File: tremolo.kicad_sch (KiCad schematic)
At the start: 29 parts, among them J1 Jack-DC, J4 Conn_01x01_Female, J5 Conn_01x01_Female, Q1 MMBT3904, SW1 SW_Push, SW2 SW_DIP_x02, U1 TAPLFO3, U2 L78L05_SOT89, U3 VTL5C, U4 TL072

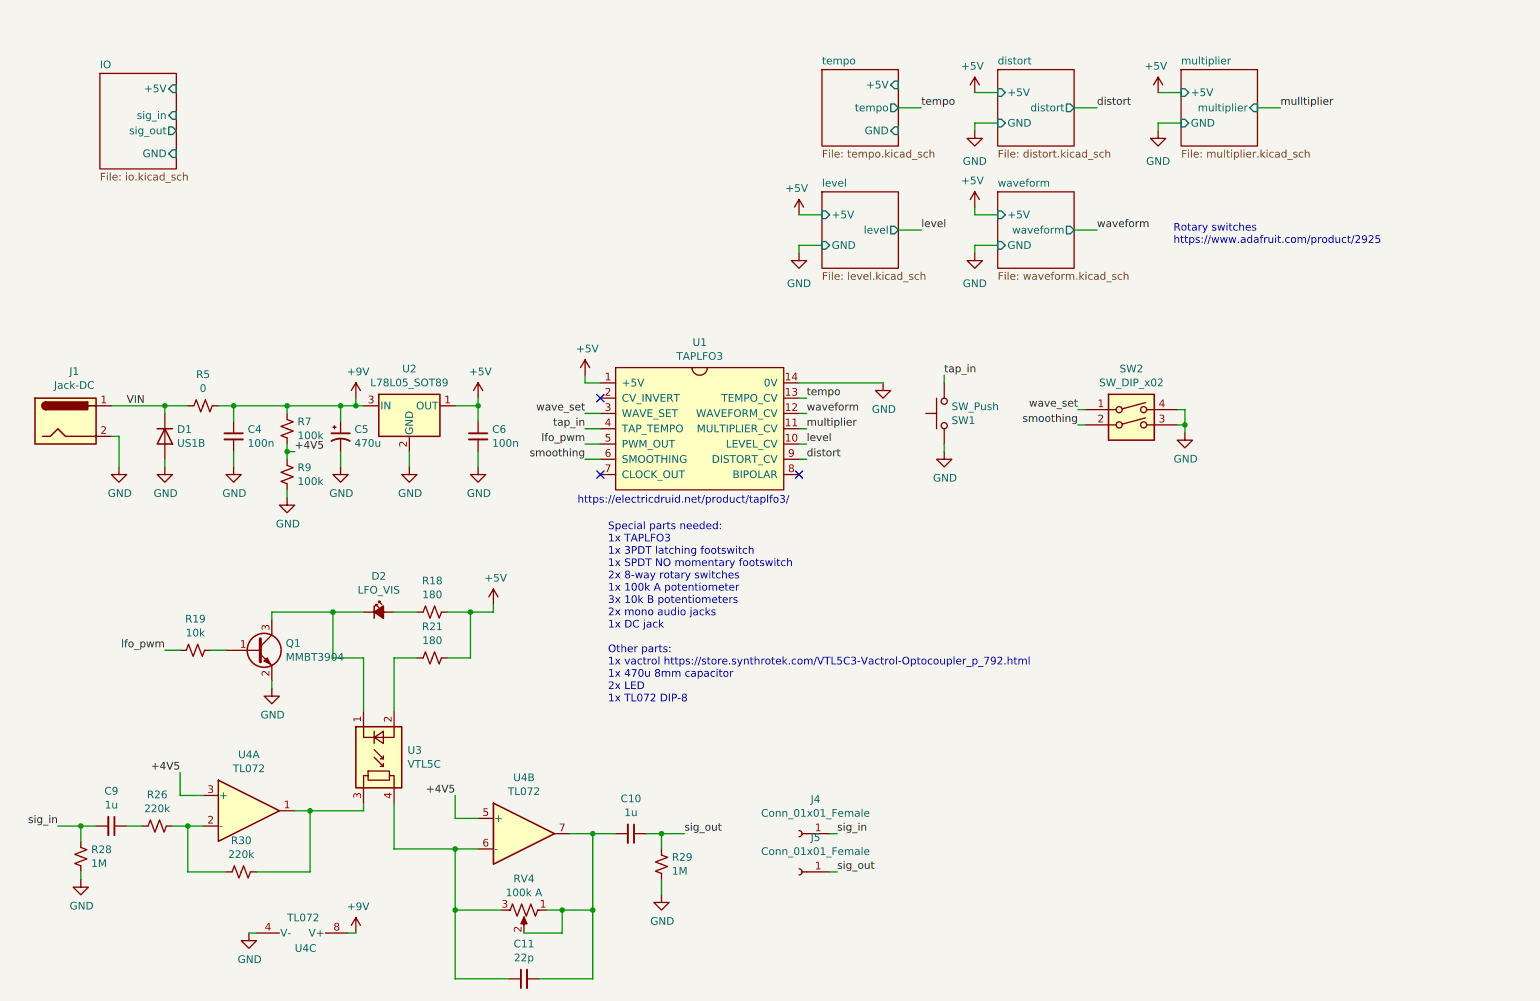
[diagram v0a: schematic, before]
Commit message: Separate IO from main board
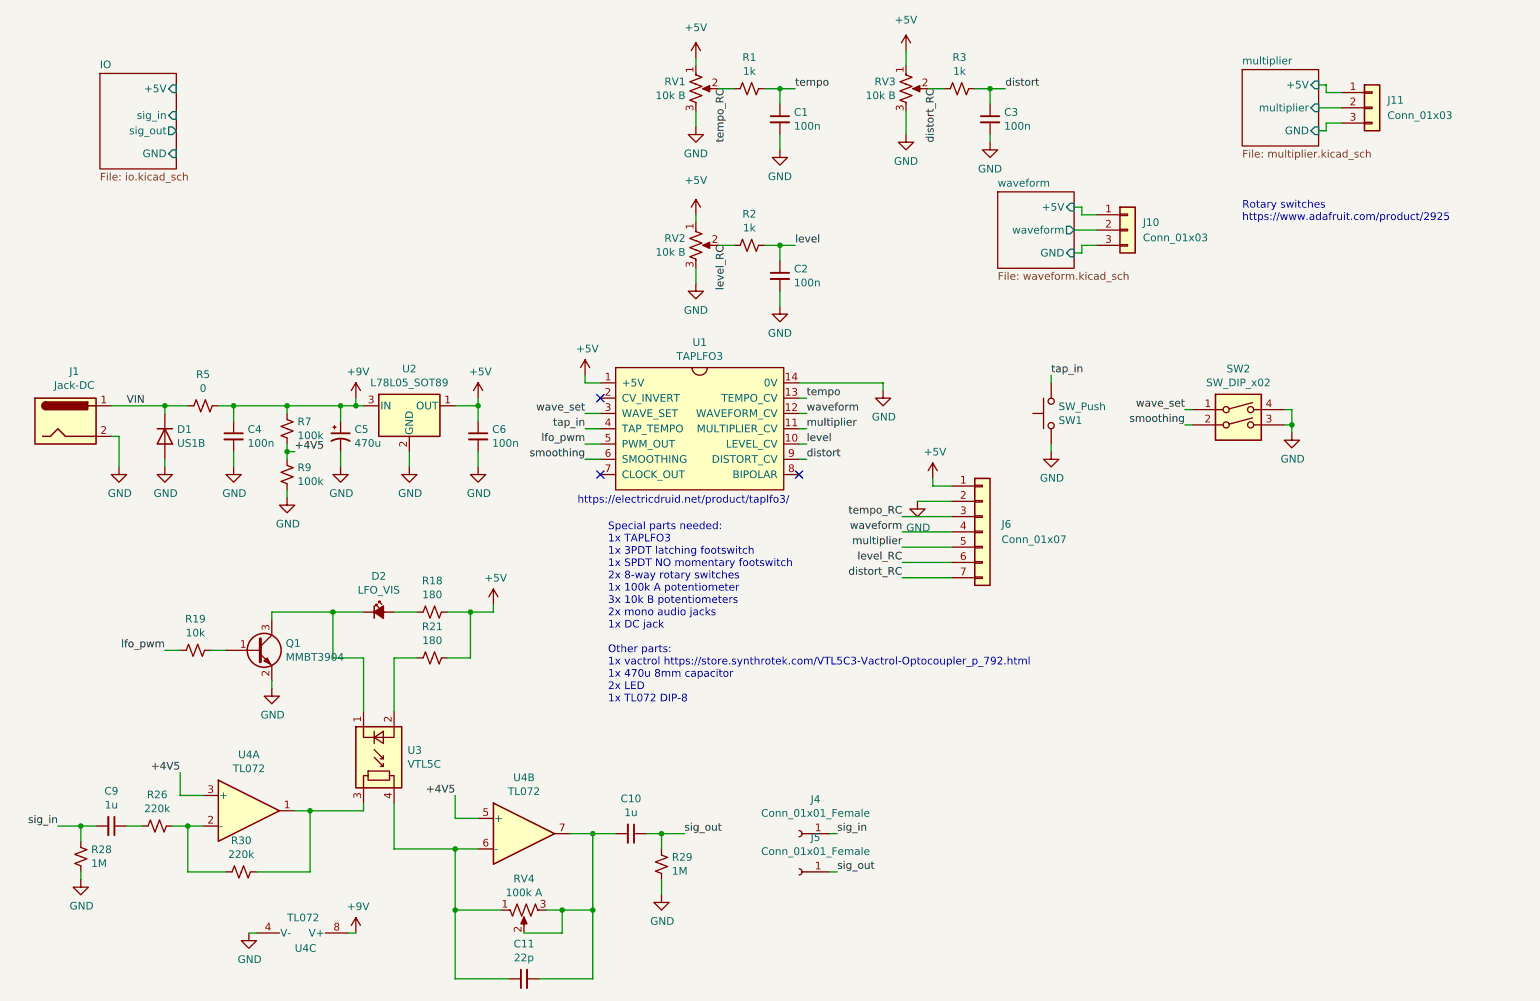
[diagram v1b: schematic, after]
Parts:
- added C1, C2, C3: 100n, Capacitor_SMD:C_0805_2012Metric, symbol Device:C_Small
- added J10, J11: Conn_01x03, Connector_PinHeader_2.54mm:PinHeader_1x03_P2.54mm_Vertical, symbol Connector_Generic:Conn_01x03
- added J6: Conn_01x07, Connector_PinHeader_2.54mm:PinHeader_1x07_P2.54mm_Vertical, symbol Connector_Generic:Conn_01x07
- added R1, R2, R3: 1k, Resistor_SMD:R_0805_2012Metric, symbol Device:R_Small_US
- added RV1, RV2, RV3: 10k B, Potentiometer_THT:Potentiometer_Alps_RK09L_Single_Vertical, symbol Device:R_Potentiometer_US
- RV4: footprint Potentiometer_THT:Potentiometer_Alps_RK09L_Single_Vertical -> Connector_PinHeader_2.54mm:PinHeader_1x02_P2.54mm_Vertical
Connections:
- net +5V: now also J6.1 (Pin_1), RV1.1, RV2.1, RV3.1
- net GND: now also C1.2, C2.2, C3.2, J6.2 (Pin_2), RV1.3, RV2.3, RV3.3
- net distort: now also C3.1, R3.2
- net level: now also C2.1, R2.2
- net multiplier: now also J6.5 (Pin_5)
- net tempo: now also C1.1, R1.2
- net waveform: now also J6.4 (Pin_4)
- net at C11.1, U3.4, U4.6 (-): now also RV4.1; no longer RV4.3
- net at C10.2, C11.2, RV4.2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: now also RV4.3; no longer RV4.1
- new net distort_RC: J6.7 (Pin_7), R3.1, RV3.2
- new net level_RC: J6.6 (Pin_6), R2.1, RV2.2
- new net multiplier/+5V: J11.1 (Pin_1)
- new net multiplier/GND: J11.3 (Pin_3)
- new net multiplier/multiplier: J11.2 (Pin_2)
- new net tempo_RC: J6.3 (Pin_3), R1.1, RV1.2
- new net waveform/+5V: J10.1 (Pin_1)
- new net waveform/GND: J10.3 (Pin_3)
- new net waveform/waveform: J10.2 (Pin_2)
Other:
- removed sheet distort
- removed sheet level
- removed sheet tempo
- moved on the sheet: RV4, SW1, SW2

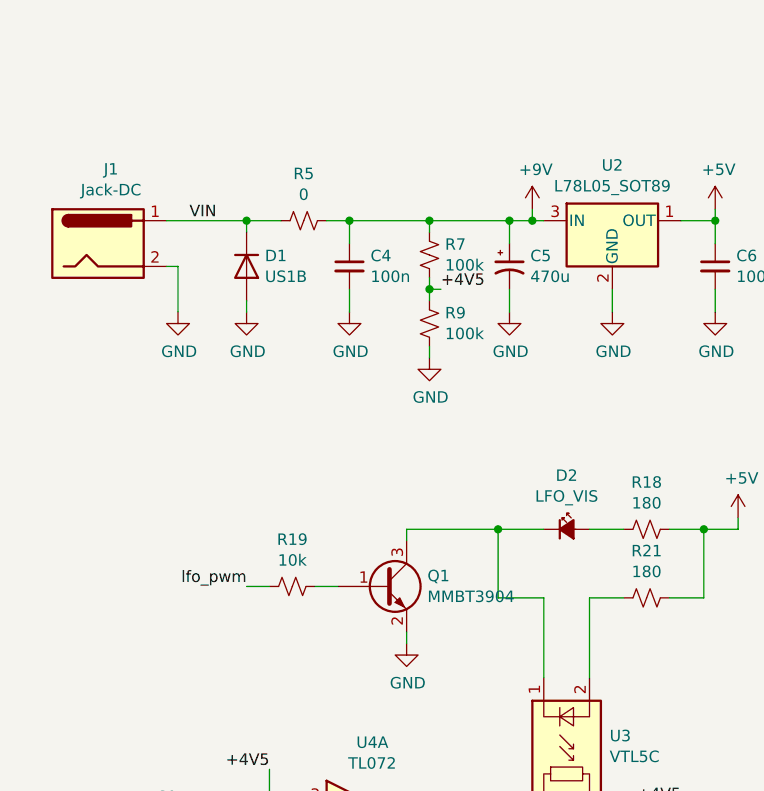
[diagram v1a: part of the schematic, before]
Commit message: THT version
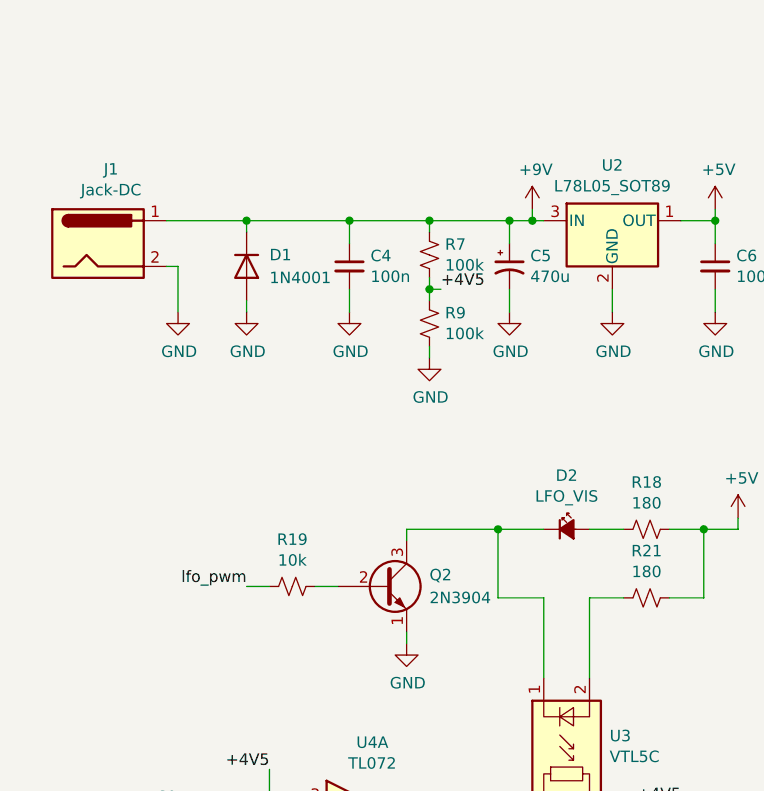
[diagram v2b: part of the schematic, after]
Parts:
- removed D1: US1B, Diode_SMD:D_SMA, symbol Diode:US1B
- removed Q1: MMBT3904, Package_TO_SOT_SMD:SOT-23, symbol Transistor_BJT:MMBT3904
- removed R5: 0, Resistor_SMD:R_0805_2012Metric, symbol Device:R_Small_US
- added D1: 1N4001, Diode_THT:D_DO-41_SOD81_P10.16mm_Horizontal, symbol Diode:1N4001
- added Q2: 2N3904, Package_TO_SOT_THT:TO-92_Inline, symbol Transistor_BJT:2N3904
- C1, C10, C11, C2, C3, C4, C6, C9: footprint Capacitor_SMD:C_0805_2012Metric -> Capacitor_THT:C_Disc_D4.3mm_W1.9mm_P5.00mm
- R1, R18, R19, R2, R21, R26, R28, R29, R3, R30, R7, R9: footprint Resistor_SMD:R_0805_2012Metric -> Resistor_THT:R_Axial_DIN0207_L6.3mm_D2.5mm_P7.62mm_Horizontal
- U2: footprint Package_TO_SOT_SMD:SOT-89-3 -> Package_TO_SOT_THT:TO-92L_Inline
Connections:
- net VIN is gone; now on net +9V: J1.1
- net +9V: now also D1.1 (K)
- net GND: now also D1.2 (A), Q2.1 (E)
- net at R19.1: now also Q2.2 (B)
- net at D2.1 (K), U3.1 (-): now also Q2.3 (C)
